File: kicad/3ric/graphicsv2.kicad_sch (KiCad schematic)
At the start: 27 parts

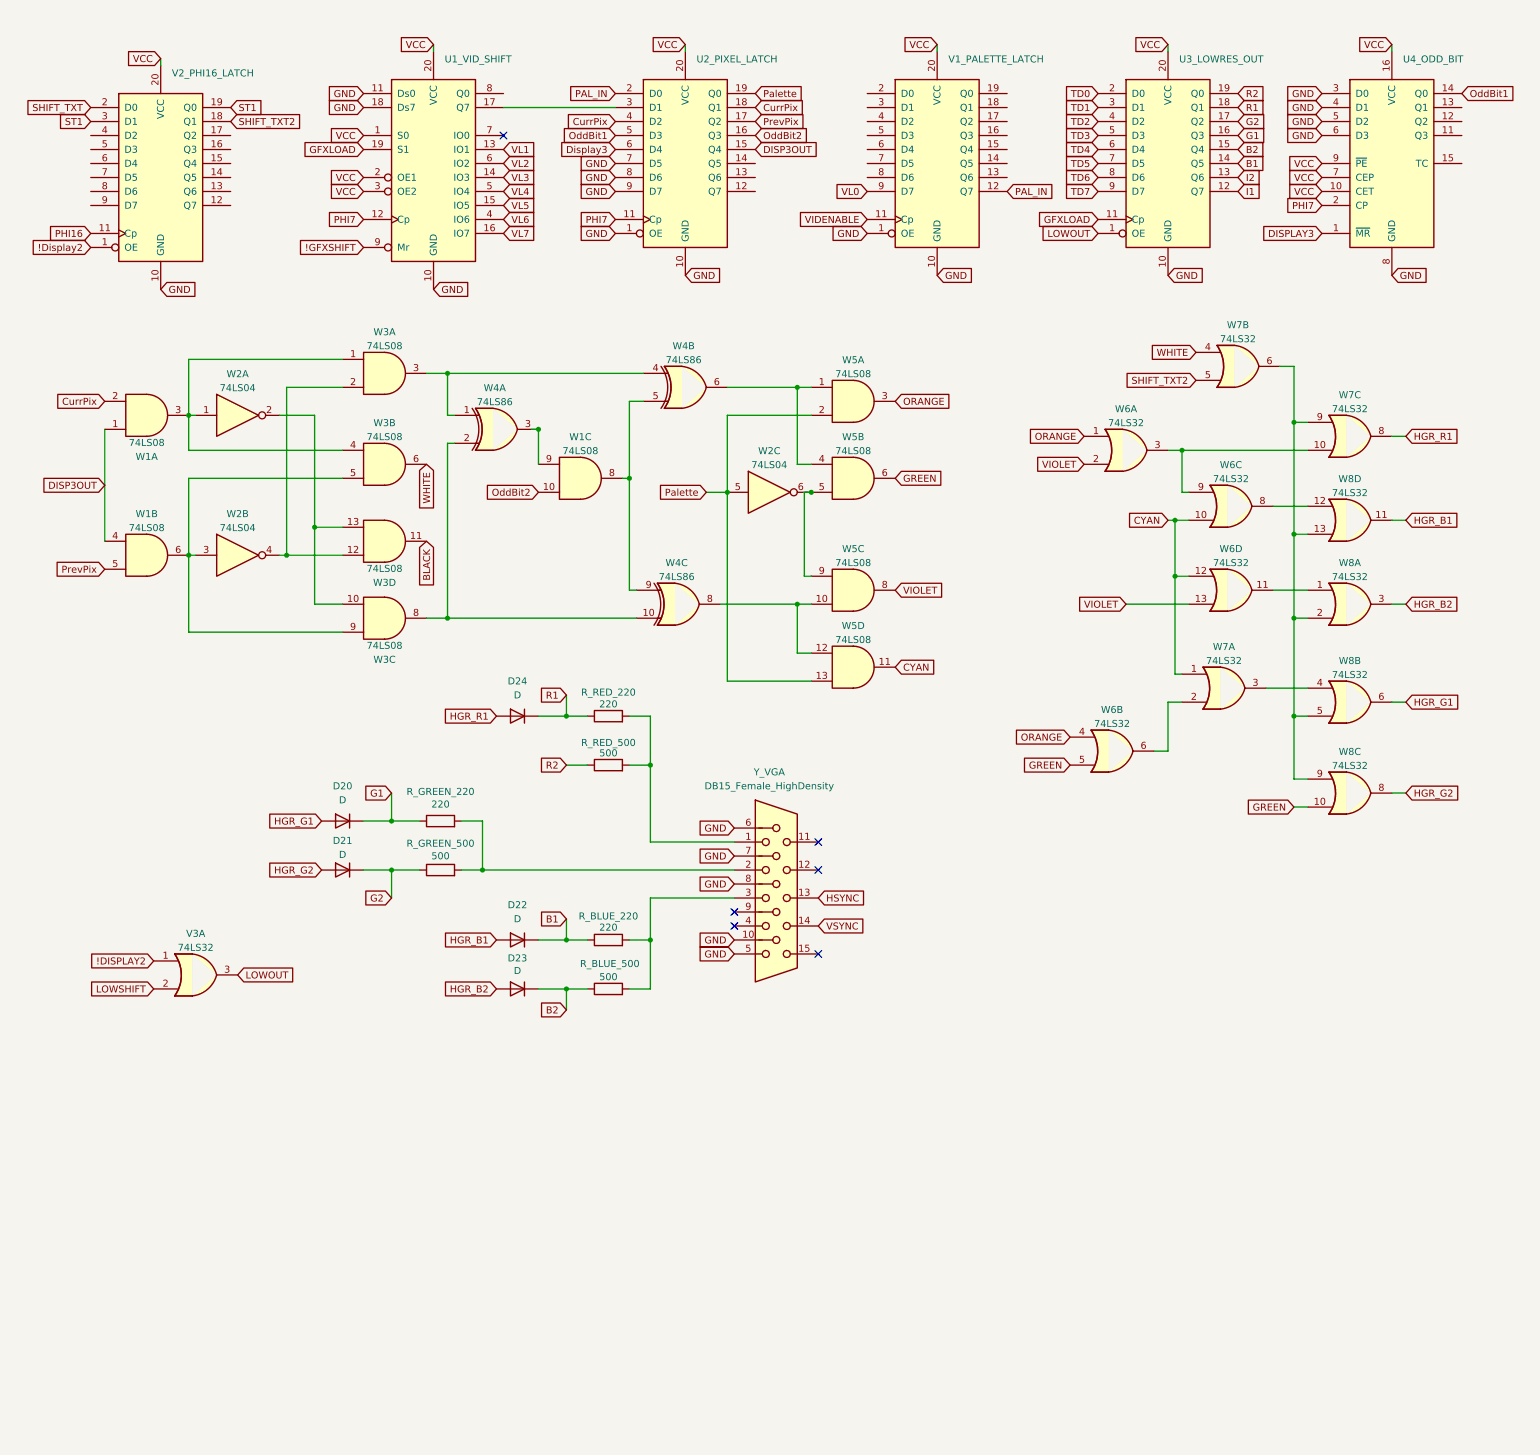
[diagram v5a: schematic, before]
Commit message: completed?  Everything wired in layout creator and first draft of completed schematic
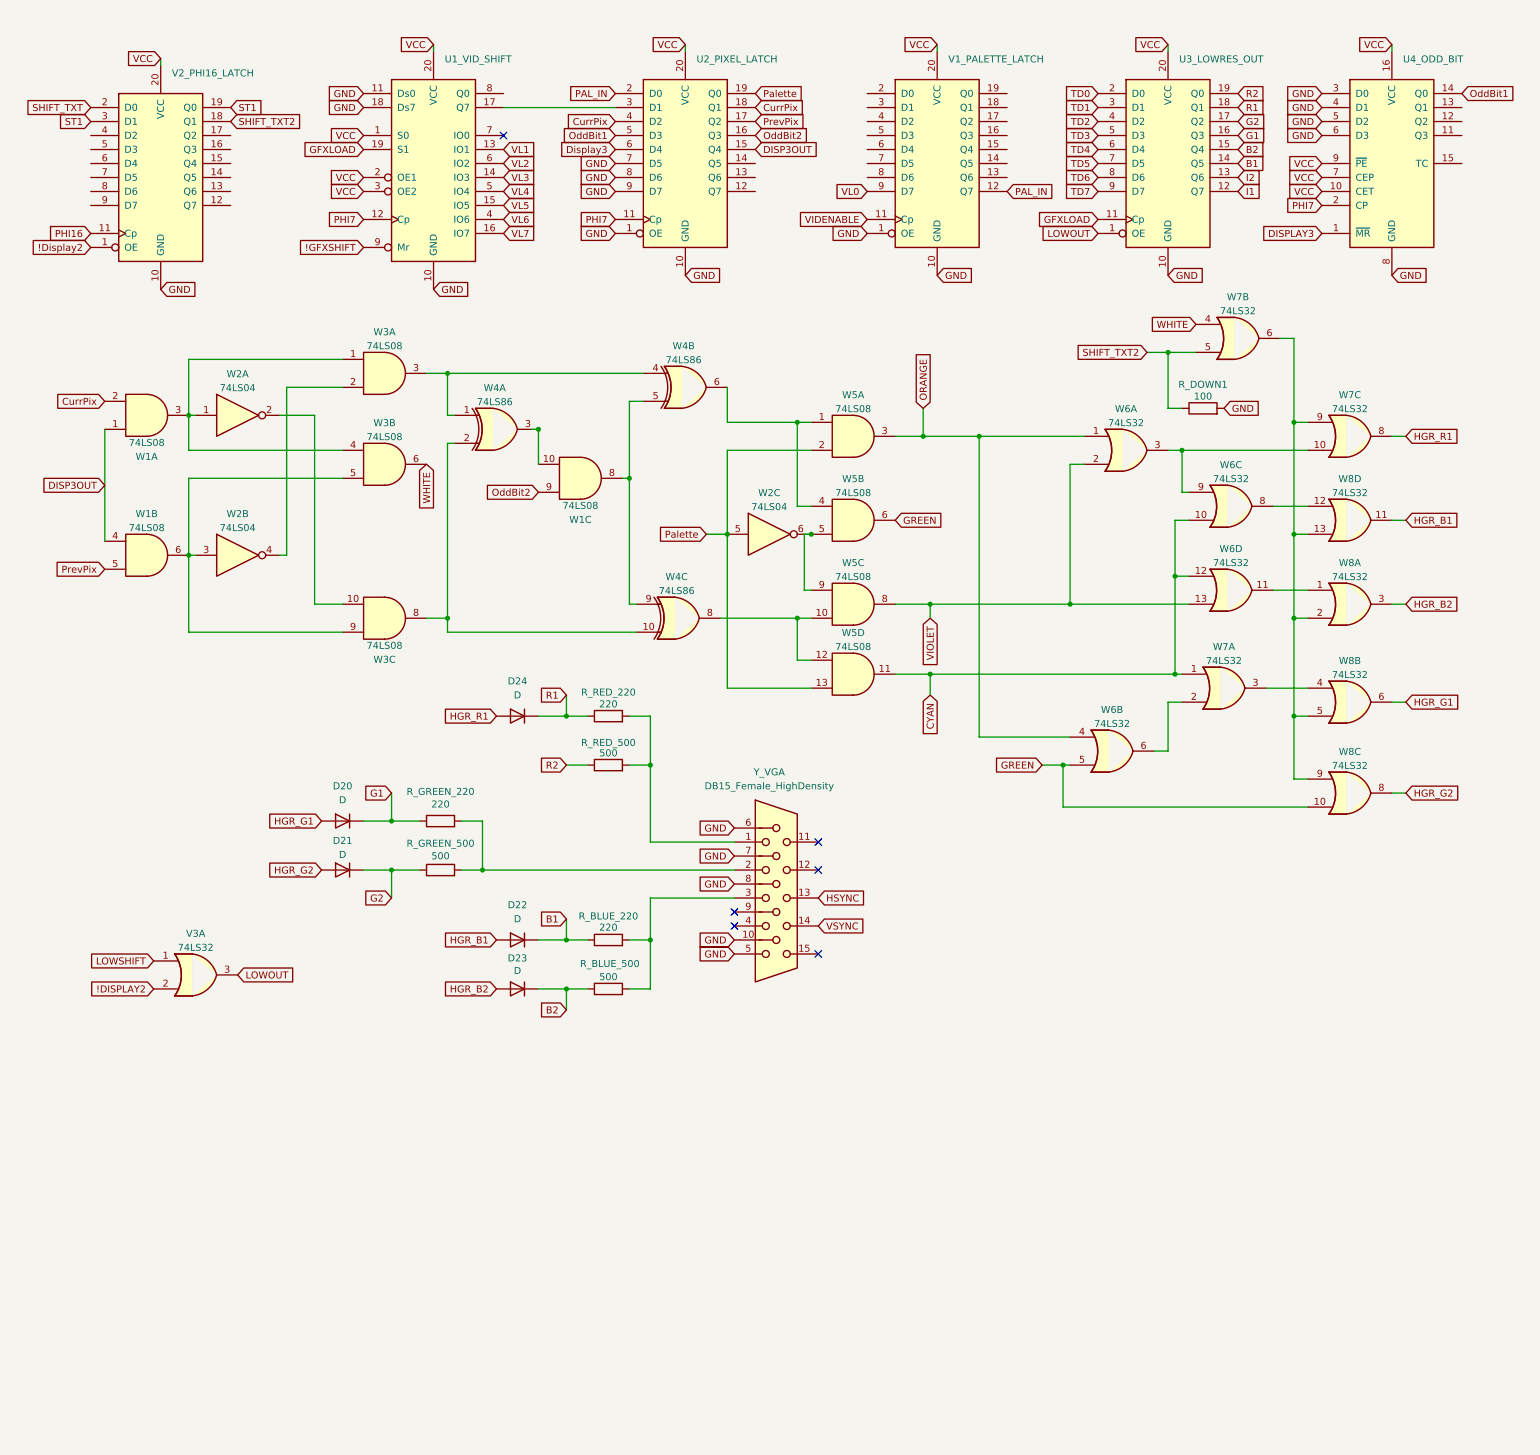
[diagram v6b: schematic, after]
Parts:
- removed unit 4 of W3
- added R_DOWN1: 100, symbol Device:R
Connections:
- net !DISPLAY2: now also V3.2; no longer V3.1
- net GND: now also R_DOWN1.2
- net LOWSHIFT: now also V3.1; no longer V3.2
- net OddBit2: now also W1.9; no longer W1.10
- net SHIFT_TXT2: now also R_DOWN1.1
- net at W4.3: now also W1.10; no longer W1.9
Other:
- moved on the sheet: W2C, W4C, W5A, W5B, W5C, W5D, W7B

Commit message: cleaning up of the schematic
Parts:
- removed V3: 74LS32, symbol 74xx:74LS32
- added unit 4 of W1
- added unit 6 of W2
- added unit 4 of W2
- added unit 5 of W2
- added unit 4 of W3
- added unit 4 of W4
- added unit 4 of W7
- D20, D21, D22, D23, D24: footprint (none) -> Diode_THT:D_A-405_P10.16mm_Horizontal
- R_BLUE_220, R_BLUE_500, R_DOWN1, R_GREEN_220, R_GREEN_500, R_RED_220, R_RED_500: footprint (none) -> Resistor_THT:R_Axial_DIN0207_L6.3mm_D2.5mm_P7.62mm_Horizontal
- U1_VID_SHIFT1: renamed from U1_VID_SHIFT; footprint (none) -> Package_DIP:DIP-20_W7.62mm_Socket
- U2_PIXEL_LATCH1: renamed from U2_PIXEL_LATCH; footprint (none) -> Package_DIP:DIP-20_W7.62mm_Socket
- U3_LOWRES_OUT1: renamed from U3_LOWRES_OUT; footprint (none) -> Package_DIP:DIP-20_W7.62mm_Socket
- U4_ODD_BIT1: renamed from U4_ODD_BIT; footprint (none) -> Package_DIP:DIP-16_W7.62mm_Socket
- V1_PALETTE_LATCH1: renamed from V1_PALETTE_LATCH; footprint (none) -> Package_DIP:DIP-20_W7.62mm_Socket
- V2_PHI16_LATCH1: renamed from V2_PHI16_LATCH; footprint (none) -> Package_DIP:DIP-20_W7.62mm_Socket
- W1, W2, W3, W4, W5, W6, W7, W8: footprint (none) -> Package_DIP:DIP-14_W7.62mm_Socket
- renumbered Y_VGA to Y_VGA1
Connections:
- net !Display2 is gone; now on net !DISPLAY2: V2_PHI16_LATCH1.1 (OE)
- net Display3 is gone; now on net DISPLAY3: U2_PIXEL_LATCH1.6 (D4)
- net !DISPLAY2: now also W7.13
- net LOWOUT: now also W7.11
- net LOWSHIFT: now also W7.12
- net I1: no longer names the net of U3_LOWRES_OUT1.12 (Q7)
- net I2: no longer names the net of U3_LOWRES_OUT1.13 (Q6)
- no-connect marks 6 -> 57

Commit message: updated schematics and PCB PNG of the breadboard layout
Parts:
- D20, D21, D22, D23, D24: footprint Diode_THT:D_A-405_P10.16mm_Horizontal -> Diode_SMD:D_SMA-SMB_Universal_Handsoldering
- R_BLUE_220, R_GREEN_220, R_RED_220: footprint Resistor_THT:R_Axial_DIN0207_L6.3mm_D2.5mm_P7.62mm_Horizontal -> Resistor_SMD:R_0603_1608Metric_Pad0.98x0.95mm_HandSolder
- R_BLUE_500, R_GREEN_500, R_RED_500: footprint Resistor_THT:R_Axial_DIN0207_L6.3mm_D2.5mm_P7.62mm_Horizontal -> Resistor_SMD:R_0805_2012Metric_Pad1.20x1.40mm_HandSolder
- R_DOWN1: footprint Resistor_THT:R_Axial_DIN0207_L6.3mm_D2.5mm_P7.62mm_Horizontal -> Resistor_SMD:R_0402_1005Metric_Pad0.72x0.64mm_HandSolder
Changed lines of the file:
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@@
 			)
 		)
-		(property "Footprint" "Diode_THT:D_A-405_P10.16mm_Horizontal"
+		(property "Footprint" "Diode_SMD:D_SMA-SMB_Universal_Handsoldering"
 			(at 102.87 189.23 0)
 			(effects
@@
 			)
 		)
-		(property "Footprint" "Resistor_THT:R_Axial_DIN0207_L6.3mm_D2.5mm_P7.62mm_Horizontal"
+		(property "Footprint" "Resistor_SMD:R_0603_1608Metric_Pad0.98x0.95mm_HandSolder"
 			(at 119.38 182.118 90)
 			(effects
@@
 			)
 		)
-		(property "Footprint" "Diode_THT:D_A-405_P10.16mm_Horizontal"
+		(property "Footprint" "Diode_SMD:D_SMA-SMB_Universal_Handsoldering"
 			(at 71.12 167.64 0)
 			(effects
@@
 			)
 		)
-		(property "Footprint" "Resistor_THT:R_Axial_DIN0207_L6.3mm_D2.5mm_P7.62mm_Horizontal"
+		(property "Footprint" "Resistor_SMD:R_0805_2012Metric_Pad1.20x1.40mm_HandSolder"
 			(at 119.38 150.368 90)
 			(effects
@@
 			)
 		)
-		(property "Footprint" "Resistor_THT:R_Axial_DIN0207_L6.3mm_D2.5mm_P7.62mm_Horizontal"
+		(property "Footprint" "Resistor_SMD:R_0603_1608Metric_Pad0.98x0.95mm_HandSolder"
 			(at 119.38 141.478 90)
 			(effects
@@
 			)
 		)
-		(property "Footprint" "Resistor_THT:R_Axial_DIN0207_L6.3mm_D2.5mm_P7.62mm_Horizontal"
+		(property "Footprint" "Resistor_SMD:R_0805_2012Metric_Pad1.20x1.40mm_HandSolder"
 			(at 88.9 169.418 90)
 			(effects
@@
 			)
 		)
-		(property "Footprint" "Diode_THT:D_A-405_P10.16mm_Horizontal"
+		(property "Footprint" "Diode_SMD:D_SMA-SMB_Universal_Handsoldering"
 			(at 71.12 158.75 0)
 			(effects
@@
 			)
 		)
-		(property "Footprint" "Diode_THT:D_A-405_P10.16mm_Horizontal"
+		(property "Footprint" "Diode_SMD:D_SMA-SMB_Universal_Handsoldering"
 			(at 102.87 180.34 0)
 			(effects
@@
 			)
 		)
-		(property "Footprint" "Diode_THT:D_A-405_P10.16mm_Horizontal"
+		(property "Footprint" "Diode_SMD:D_SMA-SMB_Universal_Handsoldering"
 			(at 102.87 139.7 0)
 			(effects
@@
 			)
 		)
-		(property "Footprint" "Resistor_THT:R_Axial_DIN0207_L6.3mm_D2.5mm_P7.62mm_Horizontal"
+		(property "Footprint" "Resistor_SMD:R_0603_1608Metric_Pad0.98x0.95mm_HandSolder"
 			(at 88.9 160.528 90)
 			(effects
@@
 			)
 		)
-		(property "Footprint" "Resistor_THT:R_Axial_DIN0207_L6.3mm_D2.5mm_P7.62mm_Horizontal"
+		(property "Footprint" "Resistor_SMD:R_0402_1005Metric_Pad0.72x0.64mm_HandSolder"
 			(at 227.33 85.598 90)
 			(effects
@@
 			)
 		)
-		(property "Footprint" "Resistor_THT:R_Axial_DIN0207_L6.3mm_D2.5mm_P7.62mm_Horizontal"
+		(property "Footprint" "Resistor_SMD:R_0805_2012Metric_Pad1.20x1.40mm_HandSolder"
 			(at 119.38 191.008 90)
 			(effects
